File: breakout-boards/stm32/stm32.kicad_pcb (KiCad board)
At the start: 2 copper layers, 29.2 x 75.6 mm, 31 parts, among them J1 Conn_ARM_JTAG_SWD_10, J2 AudioJack4, J3 CONN_LEFT, J4 CONN_RIGHT, J5 USB_SENSE, P1 USB_C, SW1 RST_SW, U1 AP2127N-3.3, U2 STM32F042K6Tx, Y1 16MHz

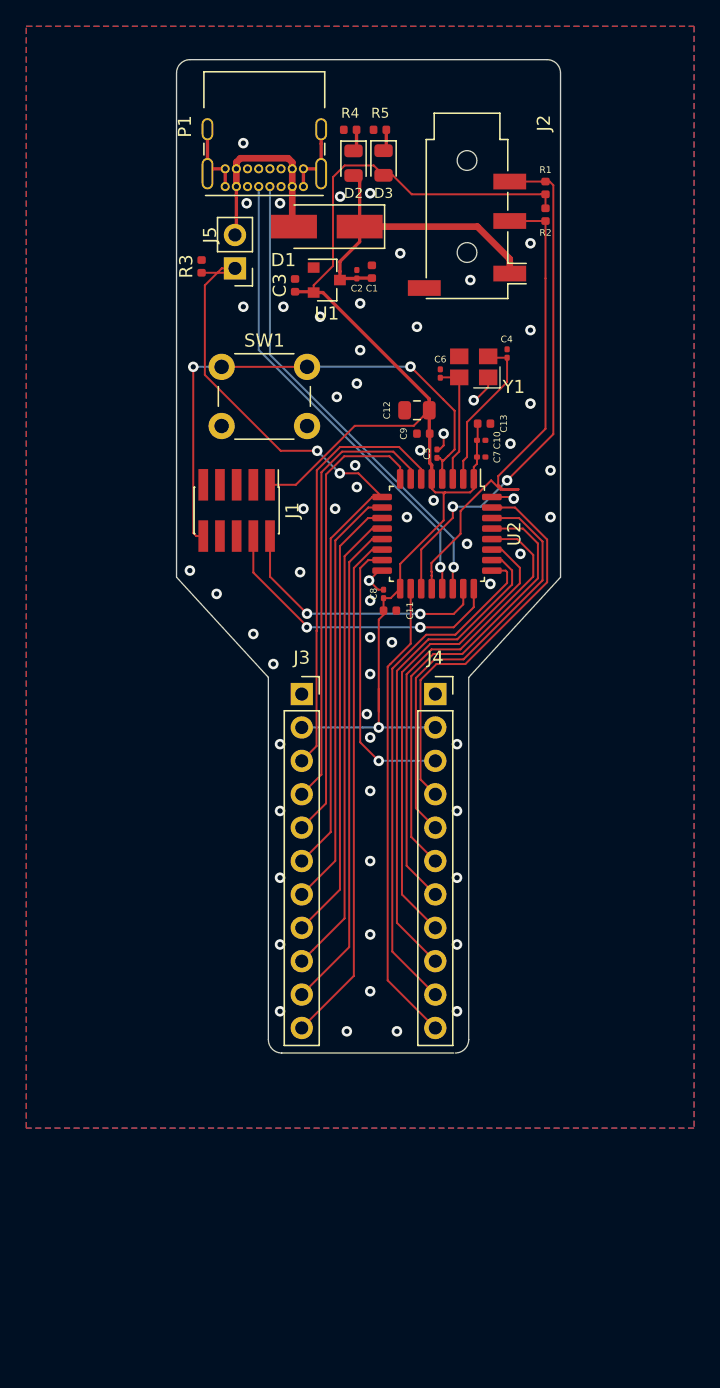
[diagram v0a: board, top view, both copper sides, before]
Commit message: (#2) add useeful silkcreen, add renders
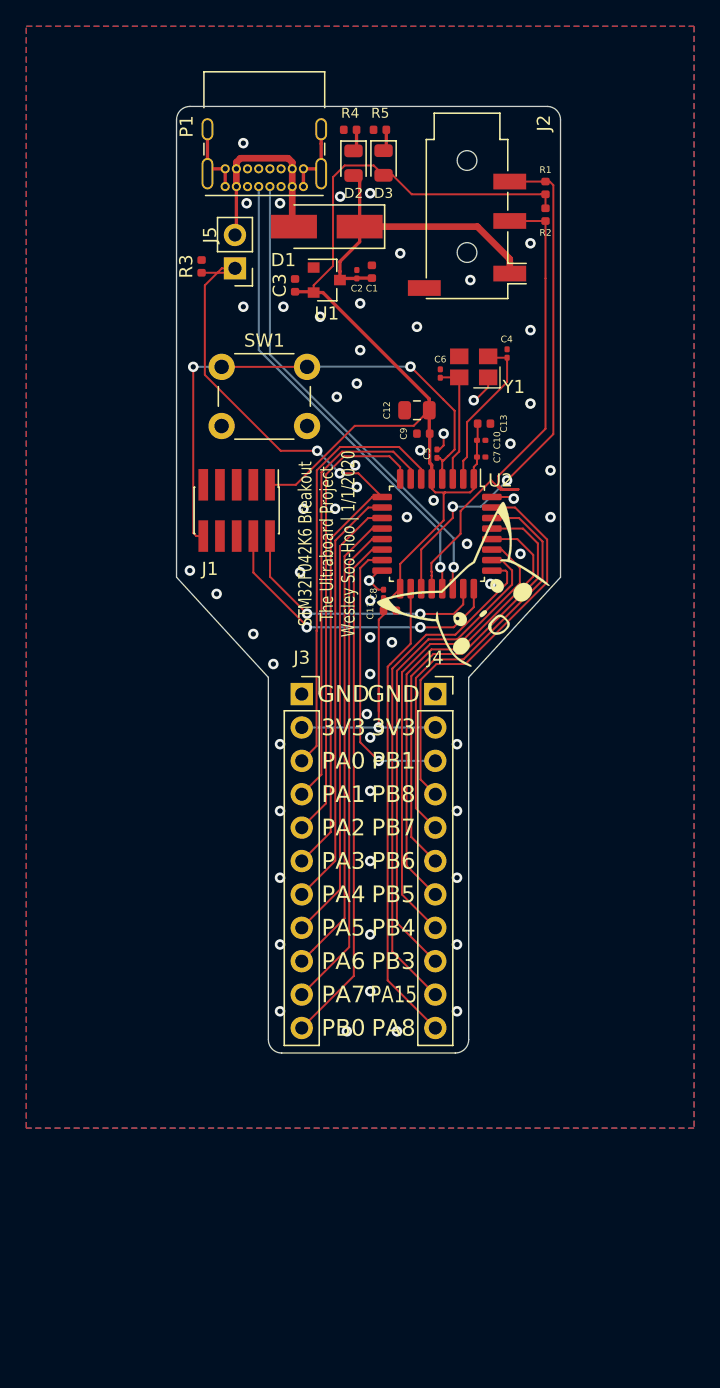
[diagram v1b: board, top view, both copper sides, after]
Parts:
- added G***: LOGO, ultraboard-img:surprised_pika, F.Cu at (135.9, 94.0)
- added G***: LOGO, ultraboard-img:michael_scott_big, B.Cu at (127.0, 97.8)
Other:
- board size 29.2 x 75.6 mm -> 29.2 x 72 mm
- board text added: "3V3"
- board text added: "GND"
- board text added: "PA0"
- board text added: "PA1"
- board text added: "PA15"
- board text added: "PA2"
- board text added: "PA3"
- board text added: "PA4"
- board text added: "PA5"
- board text added: "PA6"
- board text added: "PA7"
- board text added: "PA8"
- board text added: "PB0"
- board text added: "PB1"
- board text added: "PB3"
- board text added: "PB4"
- board text added: "PB5"
- board text added: "PB6"
- board text added: "PB7"
- board text added: "PB8"
- board text added: "STM32F042K6 Breakout The Ultraboard Project Wesley Soo-Hoo | 1/1/2020"

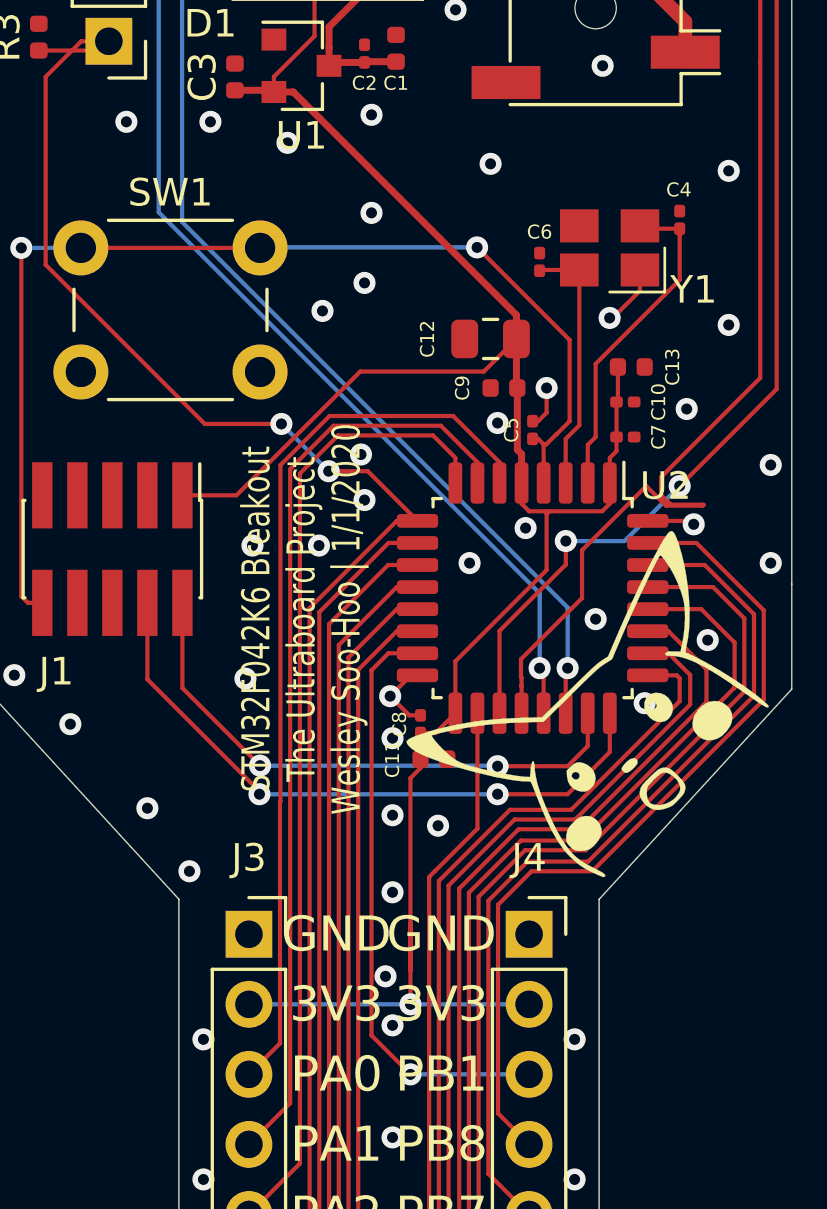
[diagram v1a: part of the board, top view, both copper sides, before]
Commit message: (#2) update silkscreen, fix stitching vias
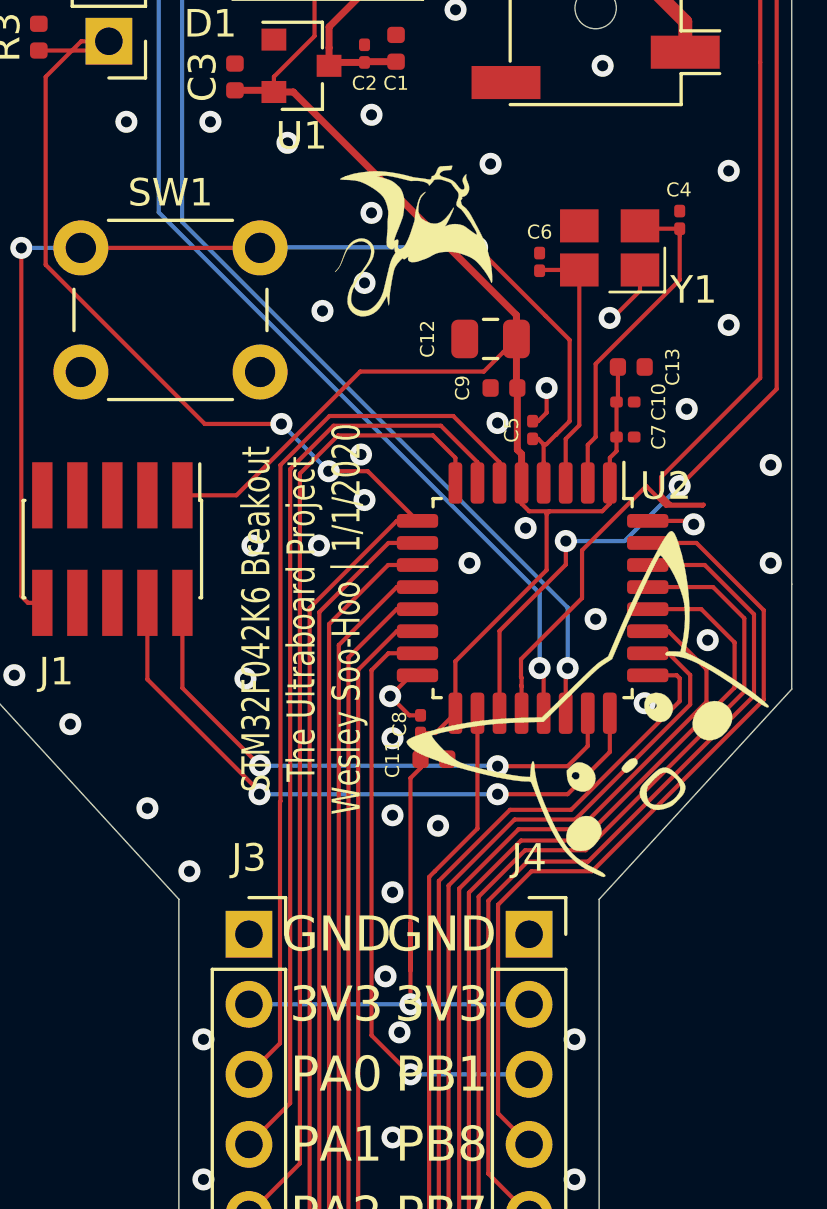
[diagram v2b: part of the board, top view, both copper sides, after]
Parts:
- added G***: LOGO, ultraboard-img:stingray, F.Cu at (128.5, 76.5)
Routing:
- net GND: vias 61 -> 62
- net (no net): vias 1 -> 0

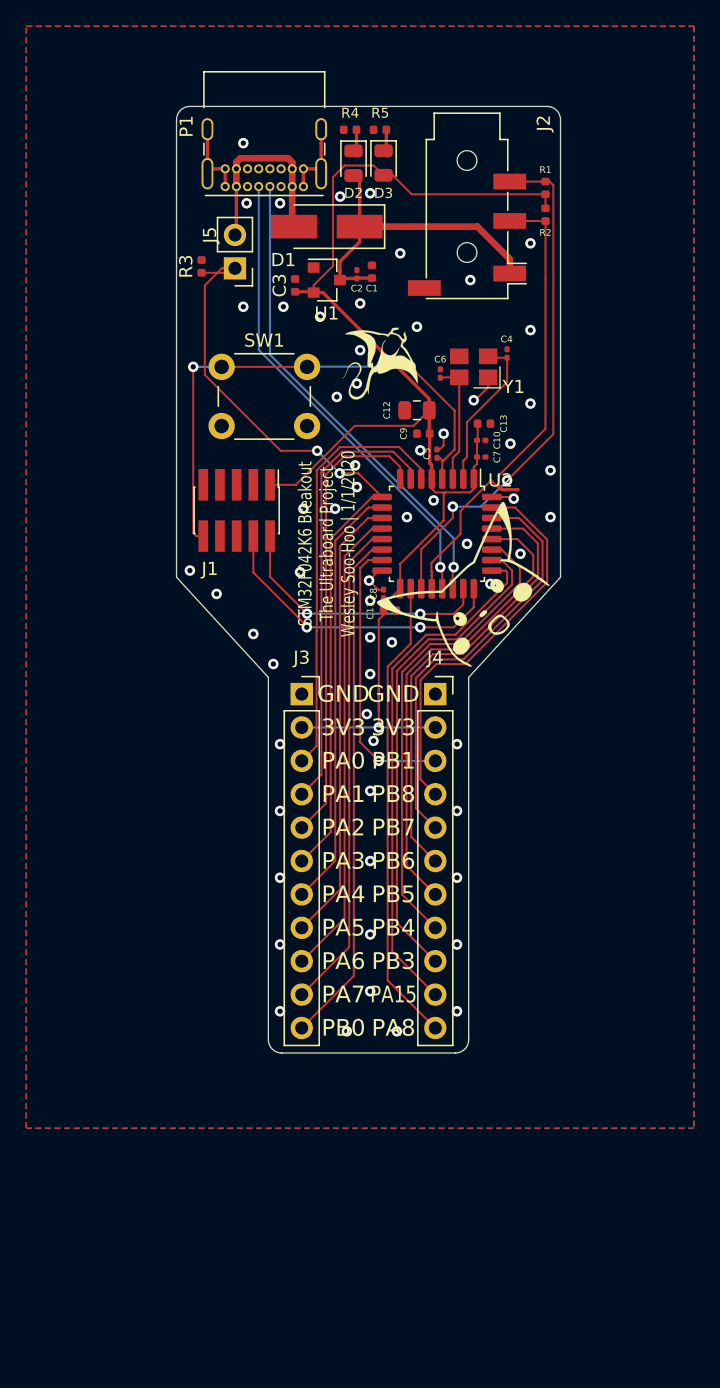
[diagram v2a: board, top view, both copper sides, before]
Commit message: (#7) Added I2C to the pin headers and switched 3v3 to 5v
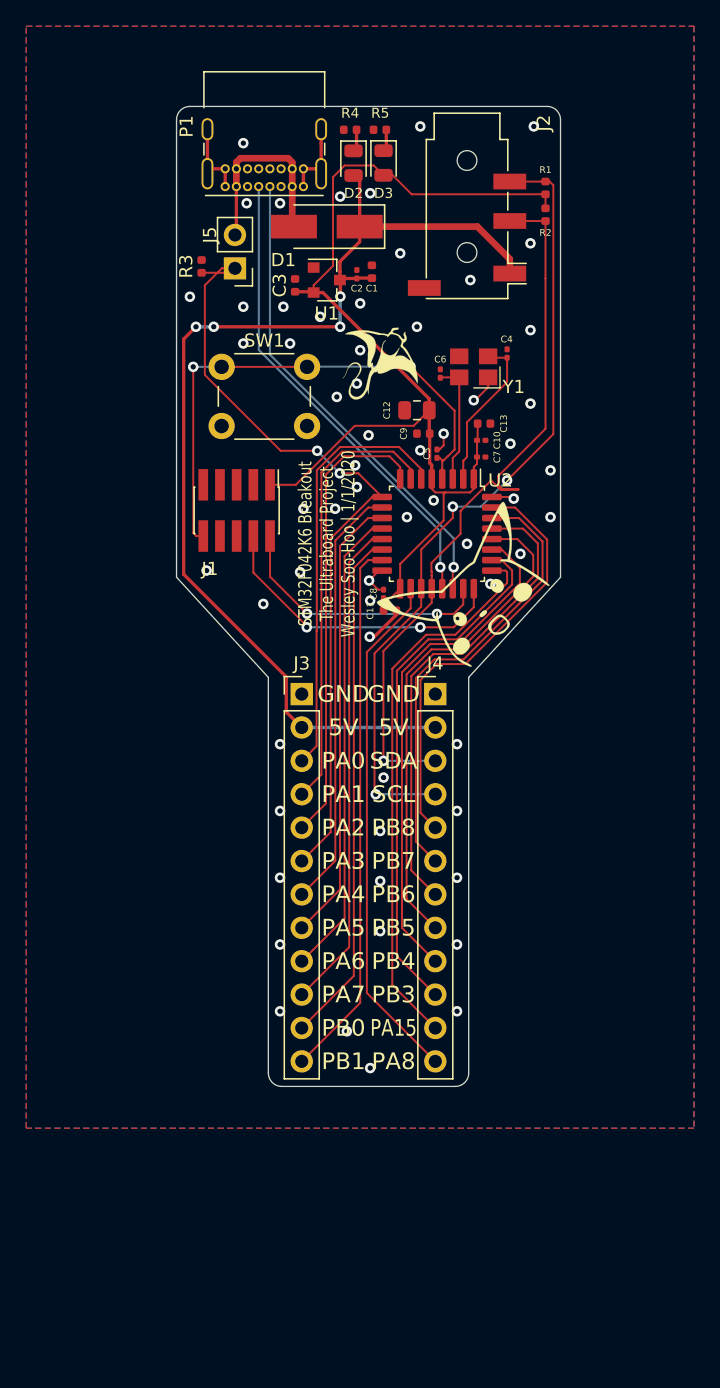
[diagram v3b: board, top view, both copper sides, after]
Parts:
- J3, J4: footprint Connector_PinSocket_2.54mm:PinSocket_1x11_P2.54mm_Vertical -> Connector_PinHeader_2.54mm:PinHeader_1x12_P2.54mm_Vertical
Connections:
- J3 pad 2: +3V3 -> VPP
- J4 pad 10: /PA15 -> /PB3
- J4 pad 11: /PA8 -> /PA15
- J4 pad 2: +3V3 -> VPP
- J4 pad 3: /PB1 -> /I2C_SDA
- J4 pad 4: /PB8 -> /I2C_SCL
- J4 pad 5: /PB7 -> /PB8
- J4 pad 6: /PB6 -> /PB7
- J4 pad 7: /PB5 -> /PB6
- J4 pad 8: /PB4 -> /PB5
- J4 pad 9: /PB3 -> /PB4
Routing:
- net VPP: track 24.8 -> 84.1 mm, vias 0 -> 4
- net /I2C_SCL: track 39.5 -> 61.2 mm, vias 2 -> 3
- net +3V3: track 103.5 -> 82.6 mm, vias 1 -> 0
- net /PB1: track 21.5 -> 41.3 mm, vias 1 -> 0
- net /I2C_SDA: track 38.5 -> 57.1 mm, vias 0 -> 1
- net /PA8: track 35.6 -> 39.5 mm
- net GND: track 20.7 -> 23.7 mm
- net /PB6: track 34.2 -> 36.7 mm
- net /PA15: track 39.6 -> 42.2 mm
- net /PB8: track 31.1 -> 33.6 mm
- net /PB4: track 36.1 -> 38.7 mm
- net /PB3: track 37.7 -> 40.3 mm
- net /PB7: track 32.3 -> 34.8 mm
- net /PB5: track 35.7 -> 38.2 mm
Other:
- board size 29.2 x 72 mm -> 29.2 x 74.5 mm
- board text added: "5V"
- board text added: "SCL"
- board text added: "SDA"
- board text removed: "3V3"

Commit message: (#14) redo stm32 and eeprom board to only include 0603 and 0805 components
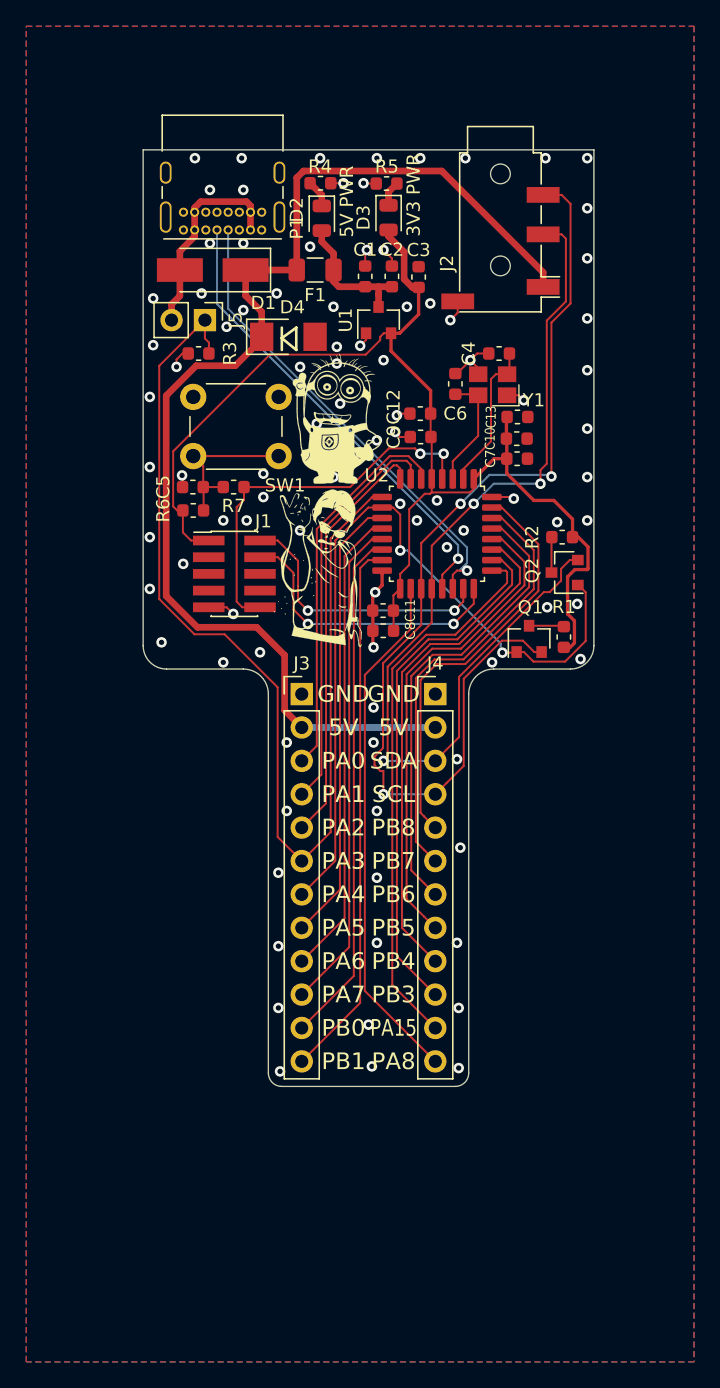
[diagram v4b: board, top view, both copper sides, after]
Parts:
- removed the G*** at (128.5, 76.5)
- added D4: ZENER, ultraboard:DO-214AA, F.Cu at (121.5, 74.4)
- added F1: 500mA, Fuse:Fuse_1206_3216Metric, F.Cu at (123.6, 69.3)
- added G***: LOGO, ultraboard-img:saltbae, F.Cu at (124.1, 91.7)
- added G***: LOGO, ultraboard-img:minion, F.Cu at (125.2, 80.6)
- added Q1: Q_NPN_BEC, Package_TO_SOT_SMD:SOT-23, F.Cu at (139.9, 97.4)
- added Q2: Q_NPN_BEC, Package_TO_SOT_SMD:SOT-23, F.Cu at (142.6, 92.4)
- added R6: R_10K, Resistor_SMD:R_0603_1608Metric, F.Cu at (114.3, 87.6)
- added R7: R_1K, Resistor_SMD:R_0603_1608Metric, F.Cu at (117.4, 85.9)
- C1, C11, C13, C3, C9: footprint Capacitor_SMD:C_0402_1005Metric -> Capacitor_SMD:C_0603_1608Metric
- C10, C2, C4, C5, C6, C7, C8: footprint Capacitor_SMD:C_0201_0603Metric -> Capacitor_SMD:C_0603_1608Metric
- C12: footprint Capacitor_SMD:C_0805_2012Metric -> Capacitor_SMD:C_0603_1608Metric
- G***: moved to B.Cu
- R1, R2, R3, R4, R5: footprint Resistor_SMD:R_0402_1005Metric -> Resistor_SMD:R_0603_1608Metric
- moved G*** 34.7 mm to (127.8, 127.7), turned to 180 degrees
- moved R1 34.2 mm to (142.5, 97.3)
- moved R2 24.6 mm to (142.4, 89.7), turned to 180 degrees
- moved C5 18.7 mm to (114.3, 85.9), turned to 180 degrees
- moved C3 9.42 mm to (131.4, 69.9)
- moved D1 9.28 mm to (115.8, 69.3)
- moved R3 6.63 mm to (114.7, 75.7), turned to 180 degrees
- moved U1 4.98 mm to (128.4, 73.2), turned to 90 degrees
- moved D2 4.84 mm to (124.1, 65.4)
- moved J1 4.83 mm to (117.4, 92.5), turned to 0 degrees
- moved R4 4.65 mm to (124.0, 62.7), turned to 0 degrees
- moved P1 4.58 mm to (119.5, 66.3)
- moved J5 4.55 mm to (115.2, 73.2), turned to 270 degrees
- moved D3 4.17 mm to (129.2, 65.4)
- moved R5 4.12 mm to (129.0, 62.8)
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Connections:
- C1 pad 1: VPP -> /5V_FUSED
- C2 pad 1: VPP -> /5V_FUSED
- C5 pad 1: /nRST -> Net-(C5-Pad1)
- D2 pad 2: VPP -> /5V_FUSED
- R1 pad 2: /I2C_SCL -> Net-(Q1-Pad3)
- R2 pad 2: /I2C_SDA -> Net-(Q2-Pad3)
- SW1 pad 1: /nRST -> GND
- SW1 pad 2: GND -> Net-(C5-Pad1)
- U1 pad 3: VPP -> /5V_FUSED
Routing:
- net /PA4: track 32.6 -> 60.1 mm, vias 0 -> 2
- net /PA3: track 60.6 -> 81.7 mm, vias 2 -> 0
- net /I2C_SCL: track 61.2 -> 77.9 mm
- net /I2C_SDA: track 57.1 -> 73.8 mm, vias 1 -> 3
- net +3V3: track 82.6 -> 95.6 mm
- net Net-(C5-Pad1): track 0.00 -> 12.5 mm
- net /nRST: track 40.9 -> 29.4 mm
- net /5V_FUSED: track 0.00 -> 10.4 mm
- net VPP: track 84.1 -> 91.3 mm, vias 4 -> 0
- net GND: track 23.7 -> 28.2 mm, vias 62 -> 96
- net /PA2: track 35.1 -> 31.8 mm
- net /PA0: track 32.7 -> 29.5 mm
- net /PA1: track 33.9 -> 30.8 mm
- net Net-(Q2-Pad3): track 0.00 -> 2.70 mm
- net Net-(Q1-Pad3): track 0.00 -> 2.67 mm
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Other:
- board size 29.2 x 74.5 mm -> 34.3 x 71.2 mm
- board text added: "3V3 PWR"
- board text added: "5V PWR"
- board text added: "STM32F042K6 Breakout | Rev. B The Ultraboard Project Wesley Soo-Hoo | 2/8/2020"
- board text removed: "STM32F042K6 Breakout The Ultraboard Project Wesley Soo-Hoo | 1/1/2020"
